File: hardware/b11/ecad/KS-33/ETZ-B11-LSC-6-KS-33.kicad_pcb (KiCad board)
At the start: 2 copper layers, 131.5 x 85.8 mm, 44 parts, among them SW1 KS-2P02B01-01-a, SW10 KS-2P02B01-01-a, SW11 KS-2P02B01-01-a, SW12 KS-2P02B01-01-a, SW13 KS-2P02B01-01-a, SW14 KS-2P02B01-01-a, SW15 KS-2P02B01-01-a, SW16 KS-2P02B01-01-a, SW17 KS-2P02B01-01-a, SW18 KS-2P02B01-01-a, SW19 KS-2P02B01-01-a, SW2 KS-2P02B01-01-a, SW20 KS-2P02B01-01-a, SW21 KS-2P02B01-01-a, SW22 KS-2P02B01-01-a, SW3 KS-2P02B01-01-a, SW4 KS-2P02B01-01-a, SW5 KS-2P02B01-01-a, SW6 KS-2P02B01-01-a, SW7 KS-2P02B01-01-a, SW8 KS-2P02B01-01-a, SW9 KS-2P02B01-01-a

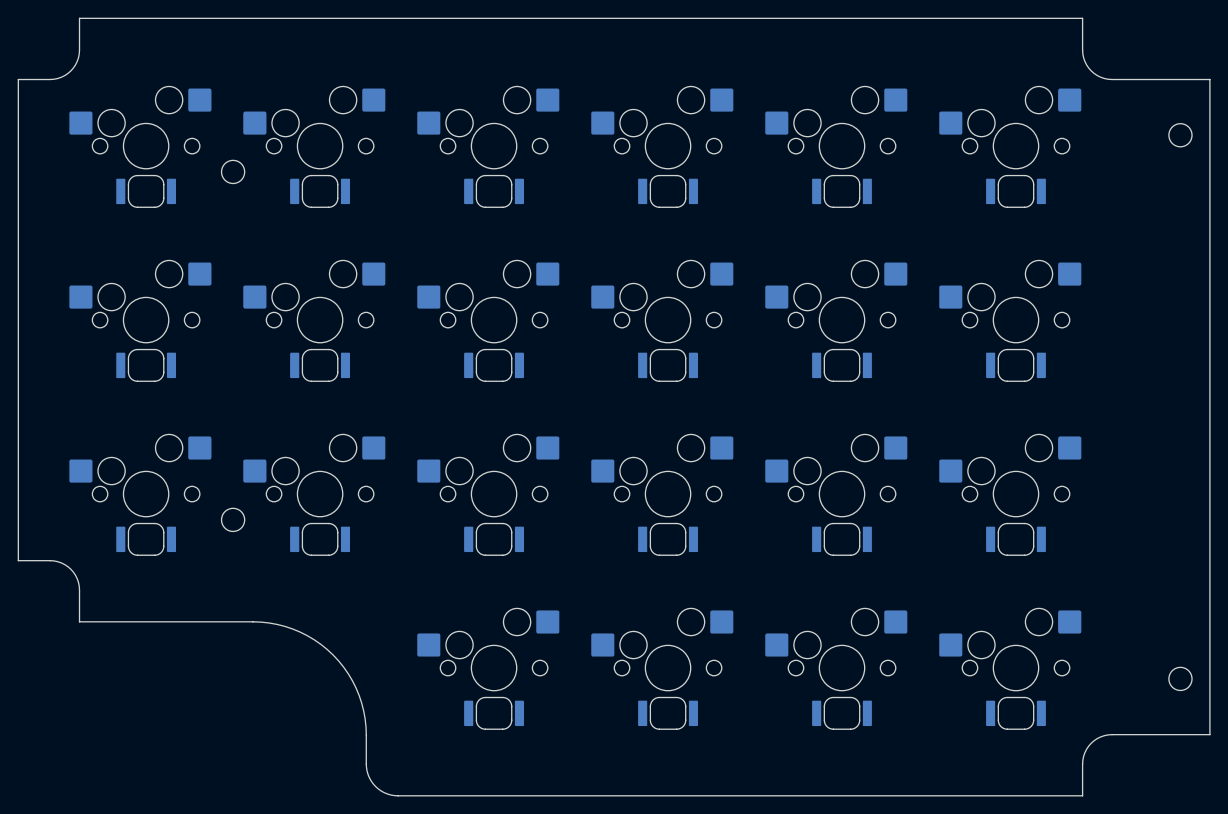
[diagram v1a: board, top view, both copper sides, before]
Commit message: feat: add B11 switch plate schematic foundation (#58)
Signed-off-by: Nikola Secerovski <secersh@gmail.com>
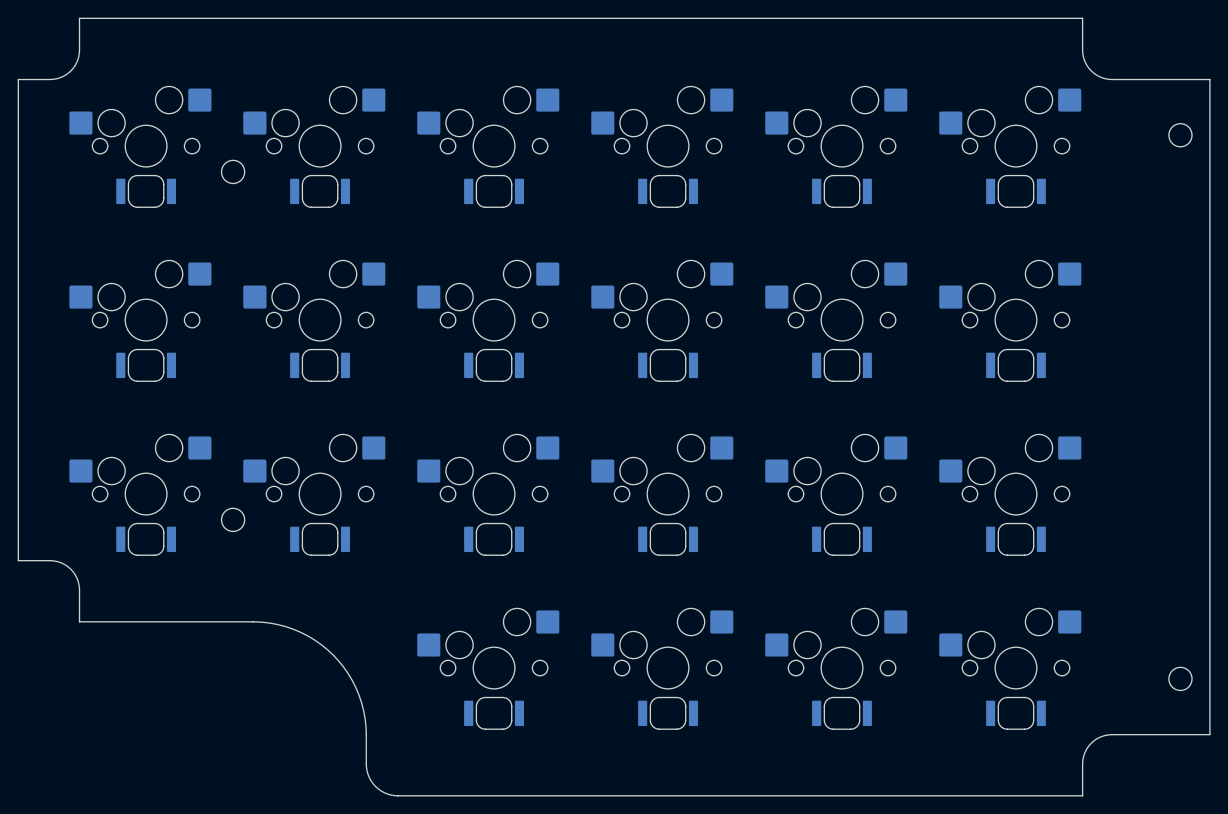
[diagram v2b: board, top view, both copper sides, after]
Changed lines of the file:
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@@
 		(pad "" np_thru_hole circle
 			(at 0 0)
-			(size 5 5)
-			(drill 5)
+			(size 4.6 4.6)
+			(drill 4.6)
 			(layers "*.Cu" "*.Mask")
 		)
@@
 		(pad "" np_thru_hole circle
 			(at 0 0)
-			(size 5 5)
-			(drill 5)
+			(size 4.6 4.6)
+			(drill 4.6)
 			(layers "*.Cu" "*.Mask")
 		)
@@
 		(pad "" np_thru_hole circle
 			(at 0 0)
-			(size 5 5)
-			(drill 5)
+			(size 4.6 4.6)
+			(drill 4.6)
 			(layers "*.Cu" "*.Mask")
 		)
@@
 		(pad "" np_thru_hole circle
 			(at 0 0)
-			(size 5 5)
-			(drill 5)
+			(size 4.6 4.6)
+			(drill 4.6)
 			(layers "*.Cu" "*.Mask")
 		)
@@
 		(pad "" np_thru_hole circle
 			(at 0 0)
-			(size 5 5)
-			(drill 5)
+			(size 4.6 4.6)
+			(drill 4.6)
 			(layers "*.Cu" "*.Mask")
 		)
@@
 		(pad "" np_thru_hole circle
 			(at 0 0)
-			(size 5 5)
-			(drill 5)
+			(size 4.6 4.6)
+			(drill 4.6)
 			(layers "*.Cu" "*.Mask")
 		)
@@
 		(pad "" np_thru_hole circle
 			(at 0 0)
-			(size 5 5)
-			(drill 5)
+			(size 4.6 4.6)
+			(drill 4.6)
 			(layers "*.Cu" "*.Mask")
 		)
@@
 		(pad "" np_thru_hole circle
 			(at 0 0)
-			(size 5 5)
-			(drill 5)
+			(size 4.6 4.6)
+			(drill 4.6)
 			(layers "*.Cu" "*.Mask")
 		)
@@
 		(pad "" np_thru_hole circle
 			(at 0 0)
-			(size 5 5)
-			(drill 5)
+			(size 4.6 4.6)
+			(drill 4.6)
 			(layers "*.Cu" "*.Mask")
 		)
@@
 		(pad "" np_thru_hole circle
 			(at 0 0)
-			(size 5 5)
-			(drill 5)
+			(size 4.6 4.6)
+			(drill 4.6)
 			(layers "*.Cu" "*.Mask")
 		)
@@
 		(pad "" np_thru_hole circle
 			(at 0 0)
-			(size 5 5)
-			(drill 5)
+			(size 4.6 4.6)
+			(drill 4.6)
 			(layers "*.Cu" "*.Mask")
 		)
@@
 		(pad "" np_thru_hole circle
 			(at 0 0)
-			(size 5 5)
-			(drill 5)
+			(size 4.6 4.6)
+			(drill 4.6)
 			(layers "*.Cu" "*.Mask")
 		)
@@
 		(pad "" np_thru_hole circle
 			(at 0 0)
-			(size 5 5)
-			(drill 5)
+			(size 4.6 4.6)
+			(drill 4.6)
 			(layers "*.Cu" "*.Mask")
 		)
@@
 		(pad "" np_thru_hole circle
 			(at 0 0)
-			(size 5 5)
-			(drill 5)
+			(size 4.6 4.6)
+			(drill 4.6)
 			(layers "*.Cu" "*.Mask")
 		)
@@
 		(pad "" np_thru_hole circle
 			(at 0 0)
-			(size 5 5)
-			(drill 5)
+			(size 4.6 4.6)
+			(drill 4.6)
 			(layers "*.Cu" "*.Mask")
 		)
@@
 		(pad "" np_thru_hole circle
 			(at 0 0)
-			(size 5 5)
-			(drill 5)
+			(size 4.6 4.6)
+			(drill 4.6)
 			(layers "*.Cu" "*.Mask")
 		)
@@
 		(pad "" np_thru_hole circle
 			(at 0 0)
-			(size 5 5)
-			(drill 5)
+			(size 4.6 4.6)
+			(drill 4.6)
 			(layers "*.Cu" "*.Mask")
 		)
@@
 		(pad "" np_thru_hole circle
 			(at 0 0)
-			(size 5 5)
-			(drill 5)
+			(size 4.6 4.6)
+			(drill 4.6)
 			(layers "*.Cu" "*.Mask")
 		)
@@
 		(pad "" np_thru_hole circle
 			(at 0 0)
-			(size 5 5)
-			(drill 5)
+			(size 4.6 4.6)
+			(drill 4.6)
 			(layers "*.Cu" "*.Mask")
 		)
@@
 		(pad "" np_thru_hole circle
 			(at 0 0)
-			(size 5 5)
-			(drill 5)
+			(size 4.6 4.6)
+			(drill 4.6)
 			(layers "*.Cu" "*.Mask")
 		)
@@
 		(pad "" np_thru_hole circle
 			(at 0 0)
-			(size 5 5)
-			(drill 5)
+			(size 4.6 4.6)
+			(drill 4.6)
 			(layers "*.Cu" "*.Mask")
 		)
@@
 		(pad "" np_thru_hole circle
 			(at 0 0)
-			(size 5 5)
-			(drill 5)
+			(size 4.6 4.6)
+			(drill 4.6)
 			(layers "*.Cu" "*.Mask")
 		)

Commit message: feat: add carrier logic FPC interconnect
Signed-off-by: Nikola Secerovski <secersh@gmail.com>
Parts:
- added J1: 503480-2000, 503480-2000, B.Cu at (212.6, 86.5)

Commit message: feat: extend B11 carrier and logic board foundations
Signed-off-by: Nikola Secerovski <secersh@gmail.com>
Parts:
- added D1: 1N4148WS, 1N4148WS, B.Cu at (86.6, 71.8)
- added D10: 1N4148WS, 1N4148WS, B.Cu at (144.2, 91.0)
- added D11: 1N4148WS, 1N4148WS, B.Cu at (163.4, 91.0)
- added D12: 1N4148WS, 1N4148WS, B.Cu at (182.6, 91.0)
- added D13: 1N4148WS, 1N4148WS, B.Cu at (86.6, 110.2)
- added D14: 1N4148WS, 1N4148WS, B.Cu at (105.8, 110.2)
- added D15: 1N4148WS, 1N4148WS, B.Cu at (125.0, 110.2)
- added D16: 1N4148WS, 1N4148WS, B.Cu at (144.2, 110.2)
- added D17: 1N4148WS, 1N4148WS, B.Cu at (163.4, 110.2)
- added D18: 1N4148WS, 1N4148WS, B.Cu at (182.6, 110.2)
- added D19: 1N4148WS, 1N4148WS, B.Cu at (125.0, 129.4)
- added D2: 1N4148WS, 1N4148WS, B.Cu at (105.8, 71.8)
- added D20: 1N4148WS, 1N4148WS, B.Cu at (144.2, 129.4)
- added D21: 1N4148WS, 1N4148WS, B.Cu at (163.4, 129.4)
- added D22: 1N4148WS, 1N4148WS, B.Cu at (182.6, 129.4)
- added D3: 1N4148WS, 1N4148WS, B.Cu at (125.0, 71.8)
- added D4: 1N4148WS, 1N4148WS, B.Cu at (144.2, 71.8)
- added D5: 1N4148WS, 1N4148WS, B.Cu at (163.4, 71.8)
- added D6: 1N4148WS, 1N4148WS, B.Cu at (182.6, 71.8)
- added D7: 1N4148WS, 1N4148WS, B.Cu at (86.6, 91.0)
- added D8: 1N4148WS, 1N4148WS, B.Cu at (105.8, 91.0)
- added D9: 1N4148WS, 1N4148WS, B.Cu at (125.0, 91.0)
- moved J1 2.01 mm to (213.1, 84.6)
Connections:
- SW1 pad 2: COL0 -> SW1
- SW10 pad 2: COL3 -> SW10
- SW11 pad 2: COL4 -> SW11
- SW12 pad 2: COL5 -> SW12
- SW13 pad 2: COL0 -> SW13
- SW14 pad 2: COL1 -> SW14
- SW15 pad 2: COL2 -> SW15
- SW16 pad 2: COL3 -> SW16
- SW17 pad 2: COL4 -> SW17
- SW18 pad 2: COL5 -> SW18
- SW19 pad 2: COL2 -> SW19
- SW2 pad 2: COL1 -> SW2
- SW20 pad 2: COL3 -> SW20
- SW21 pad 2: COL4 -> SW21
- SW22 pad 2: COL5 -> SW22
- SW3 pad 2: COL2 -> SW3
- SW4 pad 2: COL3 -> SW4
- SW5 pad 2: COL4 -> SW5
- SW6 pad 2: COL5 -> SW6
- SW7 pad 2: COL0 -> SW7
- SW8 pad 2: COL1 -> SW8
- SW9 pad 2: COL2 -> SW9
